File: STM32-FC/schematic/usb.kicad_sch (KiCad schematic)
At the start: 29 parts, among them J2 USB_C_USB2.0_14P, J3 GH 1.25mm 6P, Q2 PMDPB30XN, Q3 PMDPB55XP, U14 TPS62840, U2 USBLC6-2SC6, U3 TPS62840, U5 TPS62840

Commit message: v2.0.0 beta init
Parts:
- added J5: JST ZH 1.5mm 2P, JST_ZH:JST_ZH_S2B-ZR-SM4A-TF_1x02-1MP_P1.50mm_Horizontal, symbol Connector_Generic:Conn_01x02
- added R29: 15k, Resistor_SMD:R_0402_1005Metric, symbol Device:R_Small_US
- added R30: 1k, Resistor_SMD:R_0402_1005Metric, symbol Device:R_Small_US
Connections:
- net GND: now also J5.2 (Pin_2), R30.2
- new net +BATT: J5.1 (Pin_1), R29.1
- new net V_BATT: R29.2, R30.1
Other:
- note added: "Battery Monitoring"
- note added: "JST ZH 1.5mm 2P V_BATT : PC0 : ADC123_IN10"

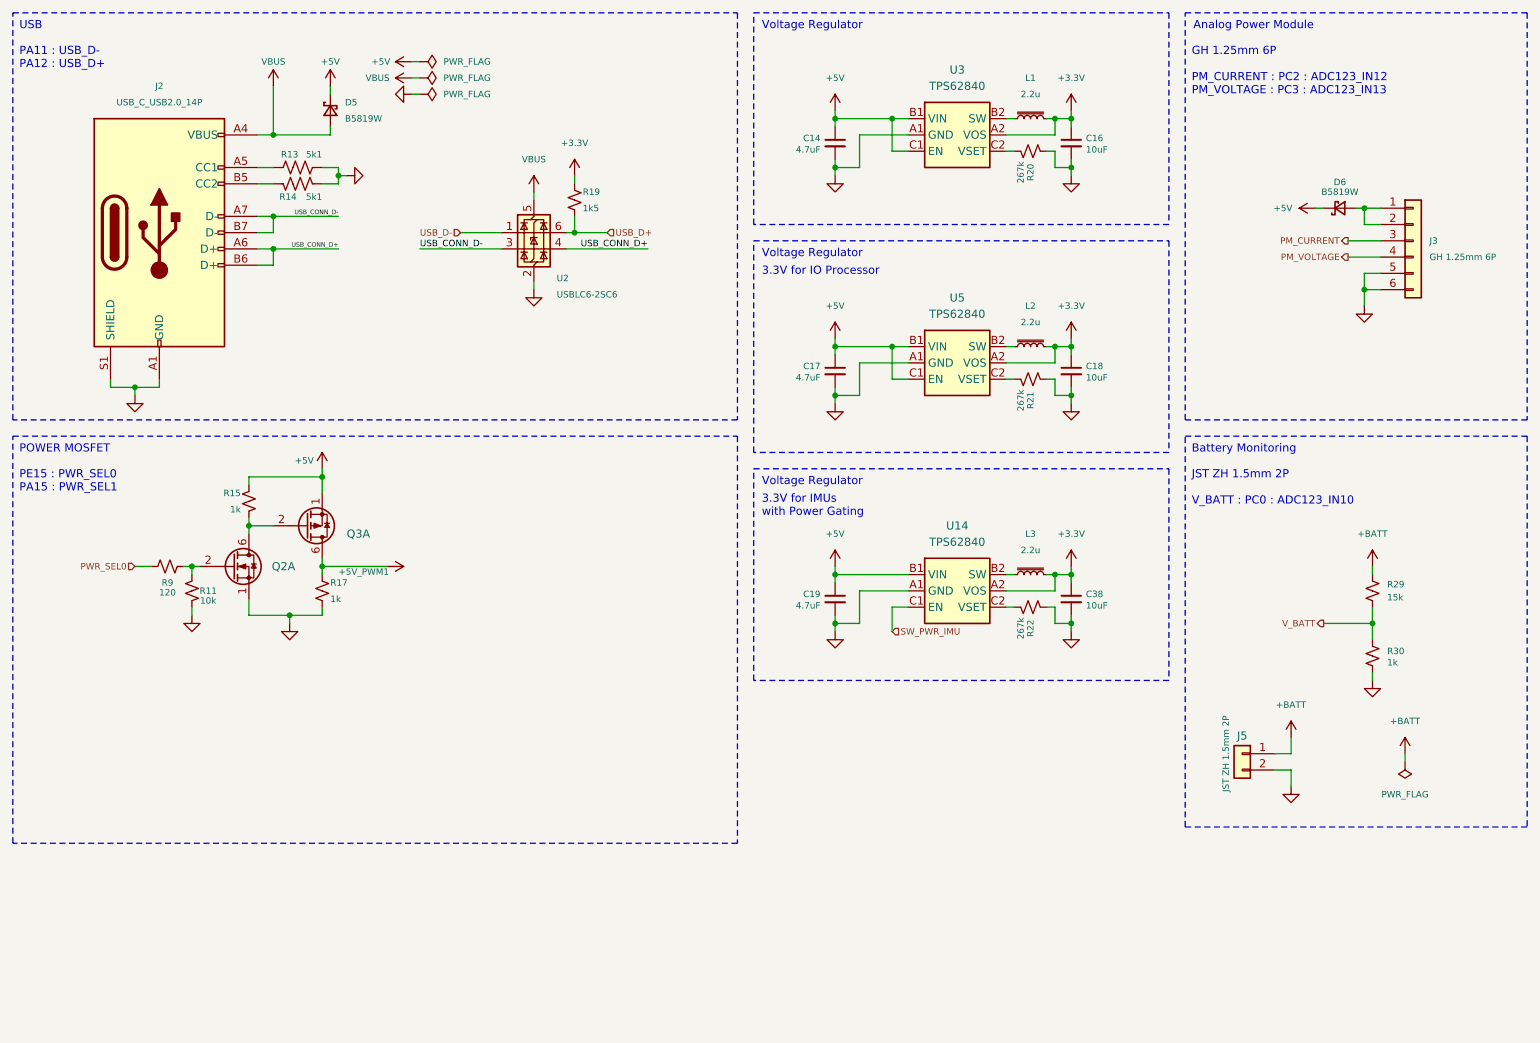
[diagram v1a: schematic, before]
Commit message: add basic circuit stm32f7
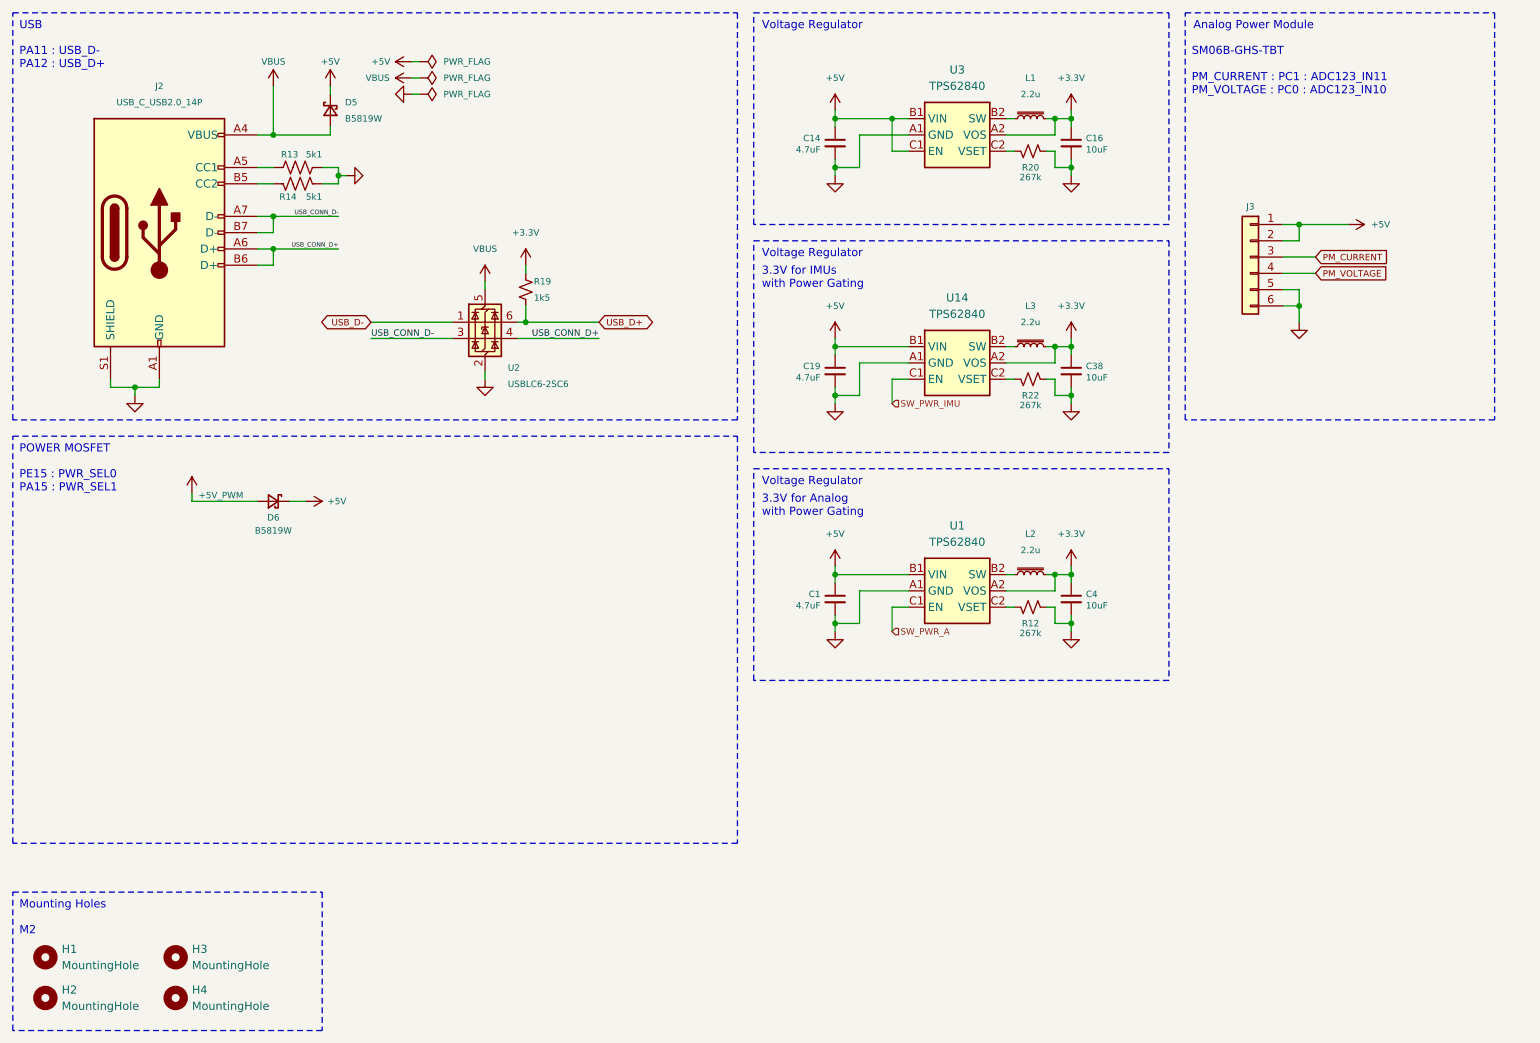
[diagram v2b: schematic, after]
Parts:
- removed C17: 4.7uF, Capacitor_SMD:C_0402_1005Metric, symbol Device:C_Small
- removed C18: 10uF, Capacitor_SMD:C_0402_1005Metric, symbol Device:C_Small
- removed J5: JST ZH 1.5mm 2P, JST_ZH:JST_ZH_S2B-ZR-SM4A-TF_1x02-1MP_P1.50mm_Horizontal, symbol Connector_Generic:Conn_01x02
- removed Q2: PMDPB30XN, Nexperia_SOT1118:Nexperia_SOT1118, symbol Nexperia_PMD:PMDPB30XN
- removed Q3: PMDPB55XP, Nexperia_SOT1118:Nexperia_SOT1118, symbol Nexperia_PMD:PMDPB55XPA
- removed R11: 10k, Resistor_SMD:R_0402_1005Metric, symbol Device:R_Small_US
- removed R15, R17, R30: 1k, Resistor_SMD:R_0402_1005Metric, symbol Device:R_Small_US
- removed R21: 267k, Resistor_SMD:R_0402_1005Metric, symbol Device:R_Small_US
- removed R29: 15k, Resistor_SMD:R_0402_1005Metric, symbol Device:R_Small_US
- removed R9: 120, Resistor_SMD:R_0402_1005Metric, symbol Device:R_Small_US
- removed U5: TPS62840, Package_BGA:Texas_DSBGA-6_0.855x1.255mm_Layout2x3_P0.4mm_LevelC, symbol TPS62840:TPS62840YBG
- added C1: 4.7uF, Capacitor_SMD:C_0402_1005Metric, symbol Device:C_Small
- added C4: 10uF, Capacitor_SMD:C_0402_1005Metric, symbol Device:C_Small
- added H1, H2, H3, H4: MountingHole, MountingHole:MountingHole_2.2mm_M2_ISO7380_Pad, symbol Mechanical:MountingHole
- added R12: 267k, Resistor_SMD:R_0402_1005Metric, symbol Device:R_Small_US
- added U1: TPS62840, Package_BGA:Texas_DSBGA-6_0.855x1.255mm_Layout2x3_P0.4mm_LevelC, symbol TPS62840:TPS62840YBG
- J3: value GH 1.25mm 6P -> SM06B-GHS-TBT
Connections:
- net +3.3V: now also C4.1, U1.A2 (VOS)
- net +5V: now also J3.1 (Pin_1), J3.2 (Pin_2), C1.1, U1.B1 (VIN)
- net GND: now also C1.2, C4.2, R12.1, U1.A1 (GND)
- net at L2.1: now also U1.B2 (SW)
- new net: R12.2, U1.C2 (VSET)
- new net +5V_PWM: D6.2 (A)
- new net SW_PWR_A: U1.C1 (EN)
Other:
- note added: "3.3V for Analog with Power Gating"
- note added: "M2"
- note added: "Mounting Holes"
- note added: "SM06B-GHS-TBT PM_CURRENT : PC1 : ADC123_IN11 PM_VOLTAGE : PC0 : ADC123_IN10"
- note removed: "3.3V for IO Processor"
- note removed: "Battery Monitoring"
- note removed: "GH 1.25mm 6P PM_CURRENT : PC2 : ADC123_IN12 PM_VOLTAGE : PC3 : ADC123_IN13"
- note removed: "JST ZH 1.5mm 2P V_BATT : PC0 : ADC123_IN10"
- moved on the sheet: C19, C38, J3, L3, R19, R22, U14, U2

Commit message: ERC passed
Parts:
- renumbered C14 to C30, C19 to C31, C1 to C32, C16 to C33, C38 to C34, C4 to C35, D6 to D5, D5 to D6, L3 to L2, L2 to L3, R19 to R10, R20 to R11, R22 to R12, R12 to R13, R13 to R8, R14 to R9, U2 to U1, U3 to U2, U14 to U3, U1 to U4
